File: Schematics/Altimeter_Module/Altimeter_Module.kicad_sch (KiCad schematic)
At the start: 104 parts, among them J1 Stack Male Edge Connector, J2 Main E-Match, J3 Drogue E-Match, J4 USB_B_Micro, J5 SWD_01x04_Pin, Q1 AO3400A, Q2 AO4406AL, Q3 AO3400A, Q4 AO3400A, Q5 AO4406AL, SW1 SW_STM_RESET, SW2 SW_STM_BOOT_MODE, U1 KX134-1211, U10 ACS70331EOLC, U12 AMS1117-3.3, U2 MS560702BA03-50, U3 W25Q128JVS, U4 LM66100DCKR, U5 LM66100DCKR, U6 STM32F103CBTx, U7 LM66100DCKR, U8 ISO1042BDWVR, U9 MPU-6050, Y1 X322516MMB4SI

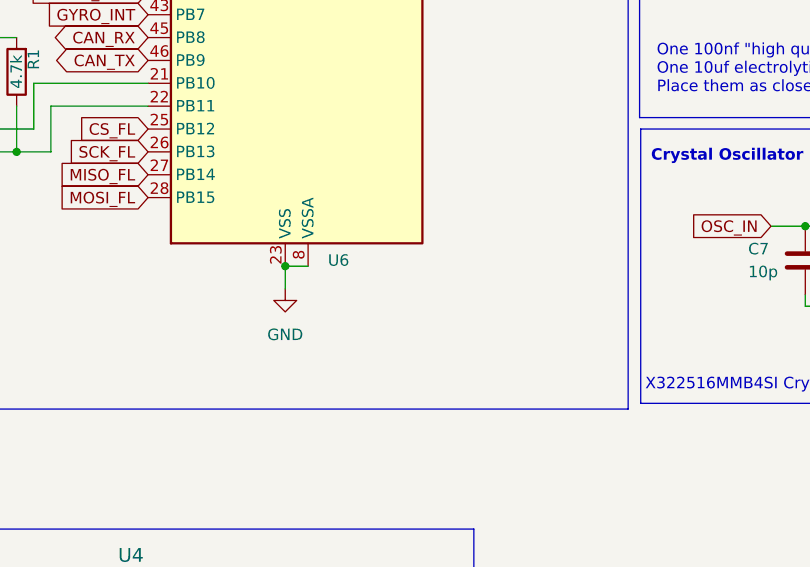
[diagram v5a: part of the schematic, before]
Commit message: Added Digikey + LCSC part numbers
Also updated MS5607 footprint to be easier to hand-solder
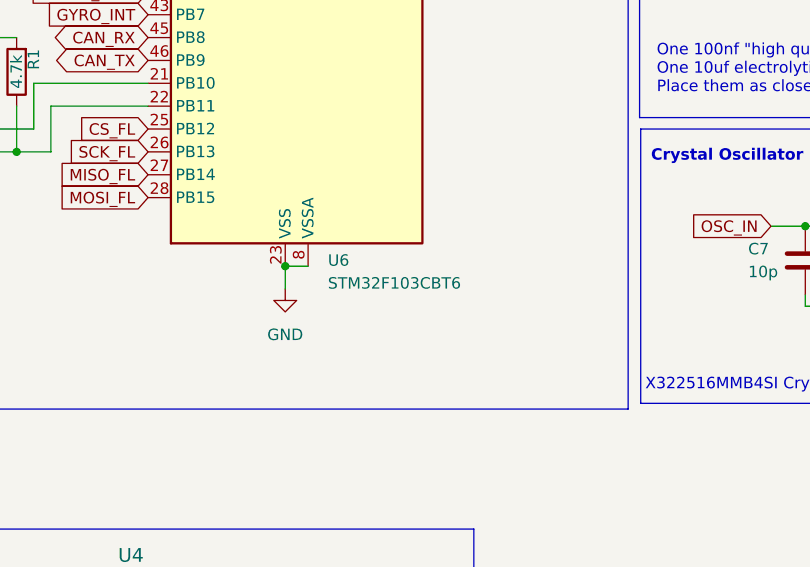
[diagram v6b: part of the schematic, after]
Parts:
- BZ2: Digikey (none) -> 490-4698-1-ND
- D2, D4: Digikey (none) -> 1568-COM-16347CT-ND
- J2, J3: Digikey 2-1445057-2 -> A33212CT-ND
- J5: Digikey (none) -> 2057-PH1RB-04-UA-ND
- U10: Digikey ACS70331EOLCTR-2P5U3 -> 620-ACS70331EOLCTR-2P5U3CT-ND
- U2: footprint digikey-footprints:SMD-8_5x3mm -> footprints:SMD-8_5x3mm_Handsolder
- U4, U5, U7: Digikey 296-53541-1-ND -> (none); LCSC (none) -> C2869734
- U6: value STM32F103CBTx -> STM32F103CBT6
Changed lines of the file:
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@@
   (title_block
     (title "QRET 23-24 SRAD Altimeter Module")
-    (date "2024-03-13")
+    (date "2024-03-18")
     (company "Queen's Rocket Engineering Team")
     (comment 1 "Contributors: Joshua Xiang, Kennan Bays")
@@
       (effects (font (size 1.27 1.27)) hide)
     )
+    (property "Digikey" "490-4698-1-ND" (at 321.945 28.575 0)
+      (effects (font (size 1.27 1.27)) hide)
+    )
     (pin "1")
     (pin "2")
@@
       (effects (font (size 1.27 1.27) italic) hide)
     )
-    (property "Digikey" "296-53541-1-ND" (at 202.565 234.315 0)
+    (property "LCSC" "C2869734" (at 202.565 234.315 0)
       (effects (font (size 1.27 1.27)) hide)
     )
@@
       (effects (font (size 1.27 1.27) italic) hide)
     )
-    (property "Digikey" "2-1445057-2" (at 97.79 20.955 0)
+    (property "Digikey" "A33212CT-ND" (at 97.79 20.955 0)
       (effects (font (size 1.27 1.27)) hide)
     )
@@
       (effects (font (size 1.27 1.27)) (justify left top) hide)
     )
+    (property "Digikey" "1568-COM-16347CT-ND" (at 54.61 38.1 0)
+      (effects (font (size 1.27 1.27)) hide)
+    )
     (pin "1")
     (pin "2")
@@
       (effects (font (size 1.27 1.27) italic) hide)
     )
-    (property "Digikey" "2-1445057-2" (at 148.59 20.955 0)
+    (property "Digikey" "A33212CT-ND" (at 148.59 20.955 0)
       (effects (font (size 1.27 1.27)) hide)
     )
@@
       (effects (font (size 1.27 1.27)) (justify left))
     )
-    (property "Value" "STM32F103CBTx" (at 224.4441 173.99 0)
-      (effects (font (size 1.27 1.27)) (justify left) hide)
+    (property "Value" "STM32F103CBT6" (at 224.4441 173.99 0)
+      (effects (font (size 1.27 1.27)) (justify left))
     )
     (property "Footprint" "Package_QFP:LQFP-48_7x7mm_P0.5mm" (at 207.01 169.545 0)
@@
       (effects (font (size 1.27 1.27)) hide)
     )
-    (property "Digikey" "ACS70331EOLCTR-2P5U3" (at 271.145 238.125 0)
+    (property "Digikey" "620-ACS70331EOLCTR-2P5U3CT-ND" (at 271.145 238.125 0)
       (effects (font (size 1.27 1.27)) hide)
     )
@@
       (effects (font (size 1.27 1.27) italic) hide)
     )
-    (property "Digikey" "296-53541-1-ND" (at 202.565 215.265 0)
+    (property "LCSC" "C2869734" (at 202.565 215.265 0)
       (effects (font (size 1.27 1.27)) hide)
     )
@@
       (effects (font (size 1.27 1.27)) hide)
     )
+    (property "Digikey" "2057-PH1RB-04-UA-ND" (at 130.81 212.725 0)
+      (effects (font (size 1.27 1.27)) hide)
+    )
     (pin "1")
     (pin "2")
@@
       (effects (font (size 1.27 1.27) italic) hide)
     )
-    (property "Digikey" "296-53541-1-ND" (at 202.565 253.365 0)
+    (property "LCSC" "C2869734" (at 202.565 253.365 0)
       (effects (font (size 1.27 1.27)) hide)
     )
@@
       (effects (font (size 1.27 1.27)) (justify left top) hide)
     )
+    (property "Digikey" "1568-COM-16347CT-ND" (at 34.29 38.1 0)
+      (effects (font (size 1.27 1.27)) hide)
+    )
     (pin "1")
     (pin "2")
@@
       (effects (font (size 1.27 1.27)) (justify left))
     )
-    (property "Footprint" "digikey-footprints:SMD-8_5x3mm" (at 38.1 143.51 0)
+    (property "Footprint" "footprints:SMD-8_5x3mm_Handsolder" (at 38.1 143.51 0)
       (effects (font (size 1.524 1.524)) (justify left) hide)
     )

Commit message: Updated MS5607 footprint + added many 3D models
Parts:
- U2: footprint footprints:SMD-8_5x3mm_Handsolder -> footprints:MS5607_Handsolder
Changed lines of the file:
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@@
       (effects (font (size 1.27 1.27)) (justify left))
     )
-    (property "Footprint" "footprints:SMD-8_5x3mm_Handsolder" (at 38.1 143.51 0)
+    (property "Footprint" "footprints:MS5607_Handsolder" (at 38.1 143.51 0)
       (effects (font (size 1.524 1.524)) (justify left) hide)
     )

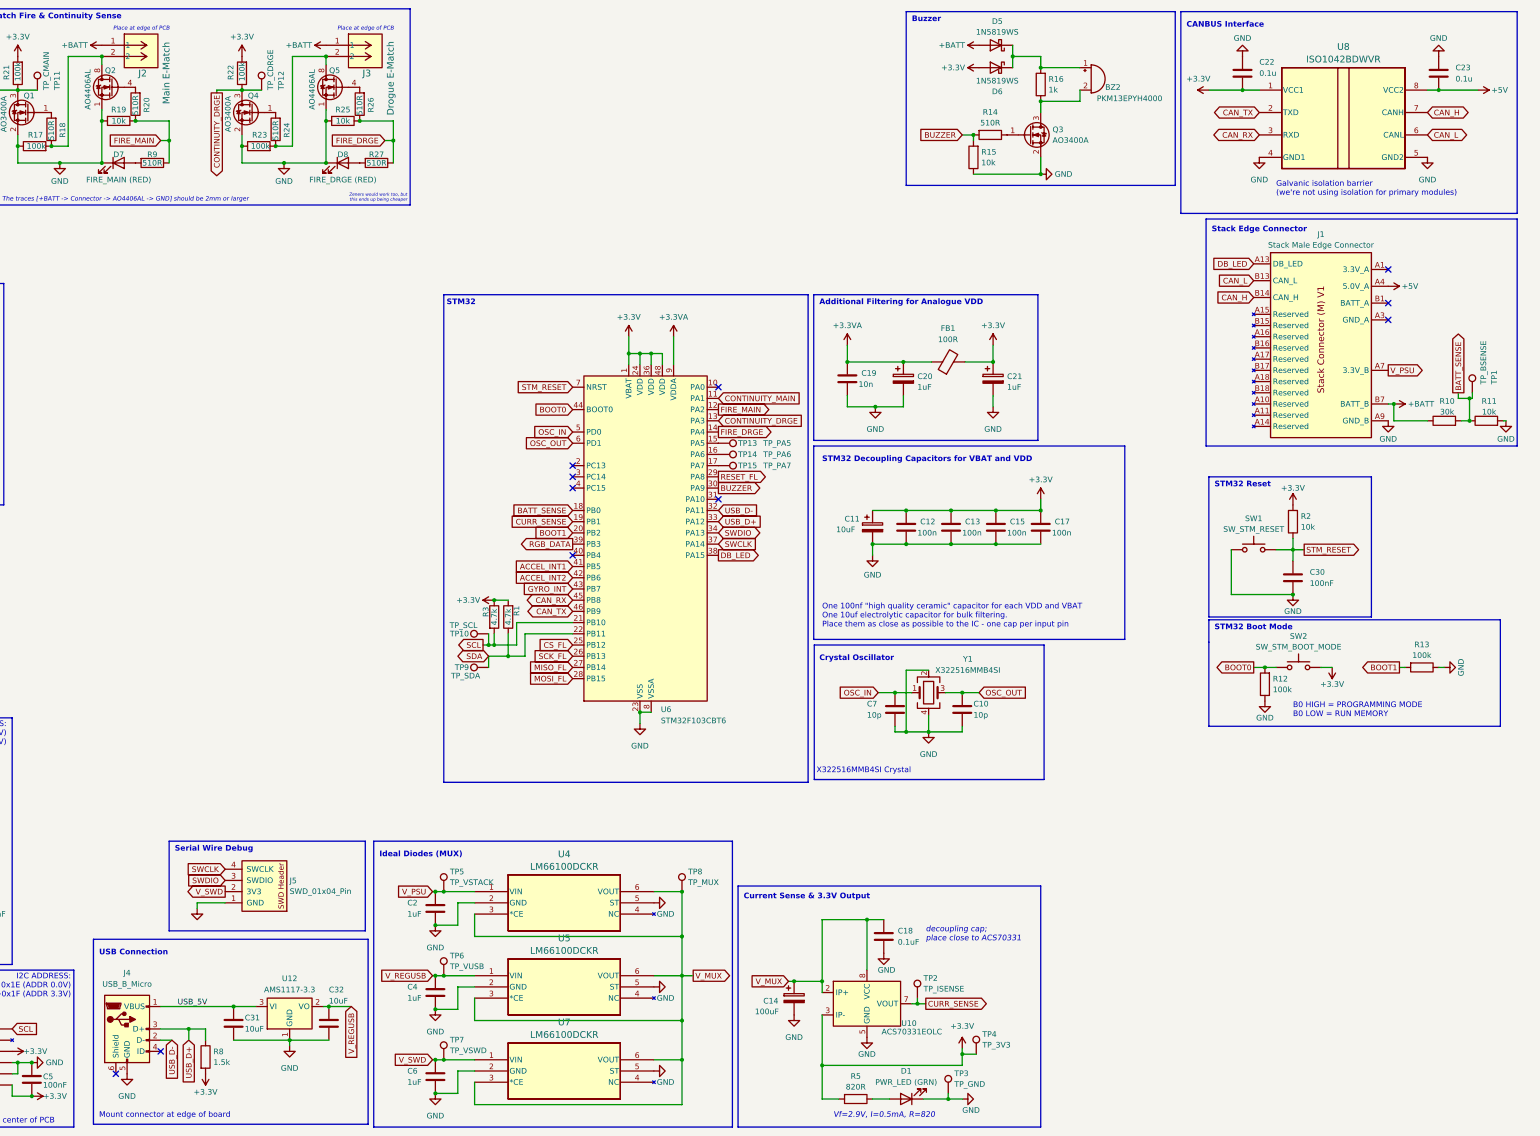
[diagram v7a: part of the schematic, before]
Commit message: Preliminary PCB layout (DRC passes)
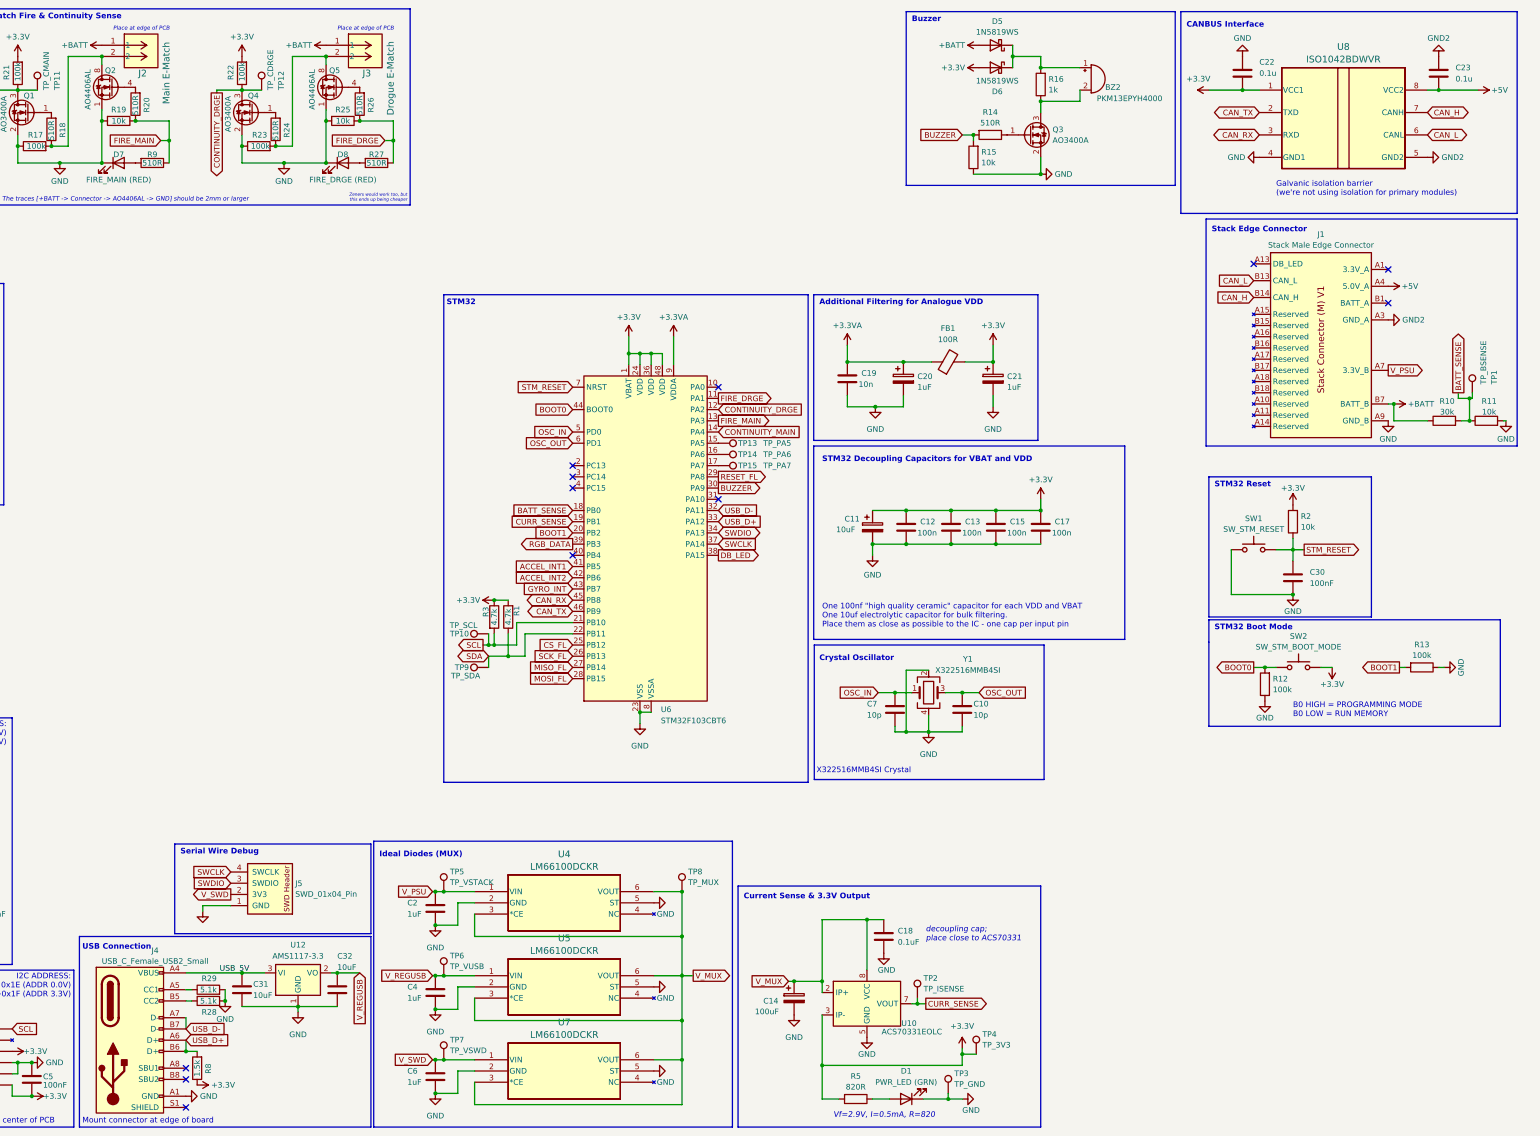
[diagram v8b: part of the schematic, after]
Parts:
- removed J4: USB_B_Micro, footprints:USB_Micro-B_Amphenol_10118194_Horizontal, symbol Connector:USB_B_Micro
- added J4: USB_C_Female_USB2_Small, footprints:USB_C_DB-108PWB, symbol USB_C:USB_C_Female_USB2_Small
- added R28, R29: 5.1k, Resistor_SMD:R_0603_1608Metric, symbol Device:R
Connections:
- net +3.3V: now also R8.1; no longer R8.2
- net CONTINUITY_DRGE: now also U6.12 (PA2); no longer U6.13 (PA3)
- net CONTINUITY_MAIN: now also U6.14 (PA4); no longer U6.11 (PA1)
- net DB_LED: no longer J1.A13 (DB_LED)
- net FIRE_DRGE: now also U6.11 (PA1); no longer U6.14 (PA4)
- net FIRE_MAIN: now also U6.13 (PA3); no longer U6.12 (PA2)
- net GND: now also J4.A1 (GND), J4.A12 (GND), J4.B1 (GND), J4.B12 (GND), R28.2, R29.2; no longer C23.1, U8.5 (GND2)
- net USB_5V: now also J4.A4 (VBUS), J4.A9 (VBUS), J4.B4 (VBUS), J4.B9 (VBUS)
- net USB_D+: now also R8.2, J4.A6 (D+), J4.B6 (D+); no longer R8.1
- net USB_D-: now also J4.A7 (D-), J4.B7 (D-)
- net GND2: now reaches J1.A3 (GND_A), J1.A6 (GND_A), J1.B4 (GND_A), J1.B5 (GND_A), J1.B6 (GND_A)
- net GND2: now also C23.1, U8.5 (GND2)
- new net: J4.A5 (CC1), R29.1
- new net: J4.B5 (CC2), R28.1
- no-connect marks 16 -> 17
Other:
- moved on the sheet: C31, C32, J5, R8, U12
